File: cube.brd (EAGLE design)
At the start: 27.9 x 59.7 mm, 46 parts, among them CN1 4U#20329, IC3 ATSAMD21E, Q2 reset, U1 AP2112K-3.3

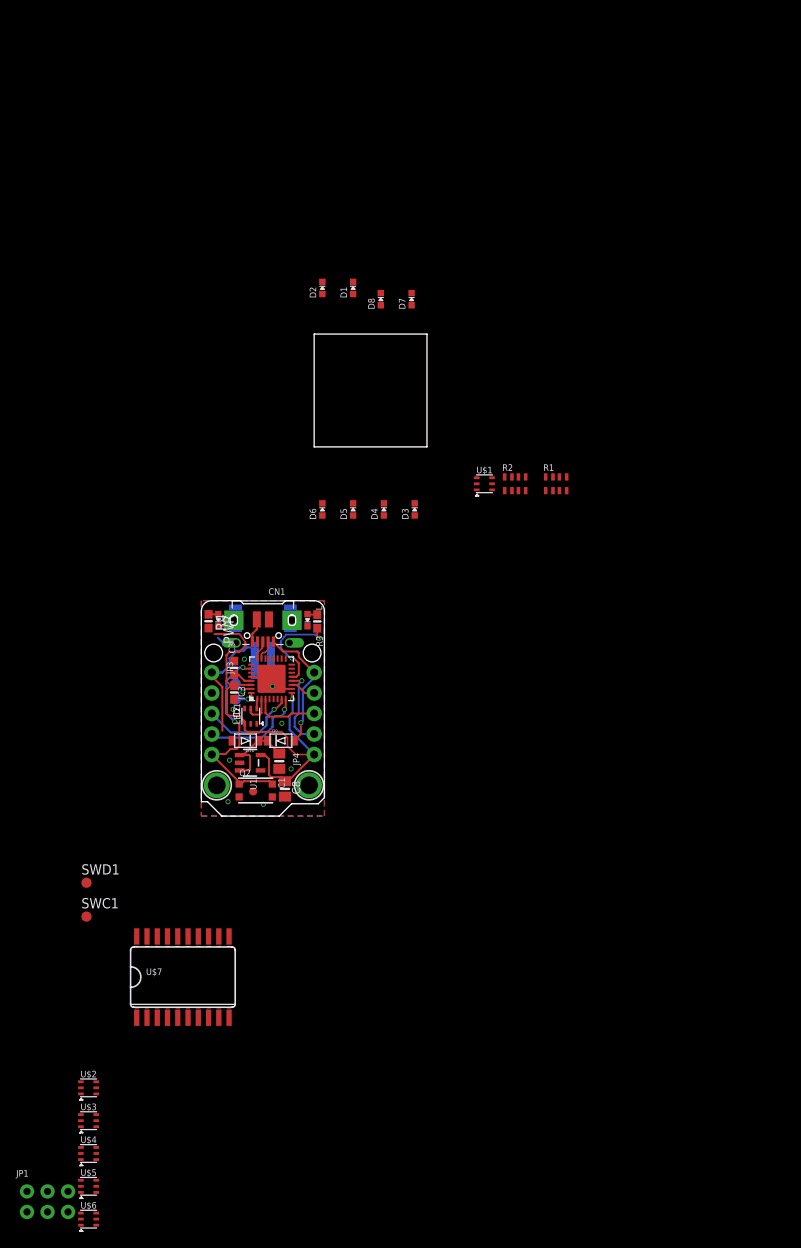
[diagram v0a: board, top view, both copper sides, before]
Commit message: made LED7 also a power led
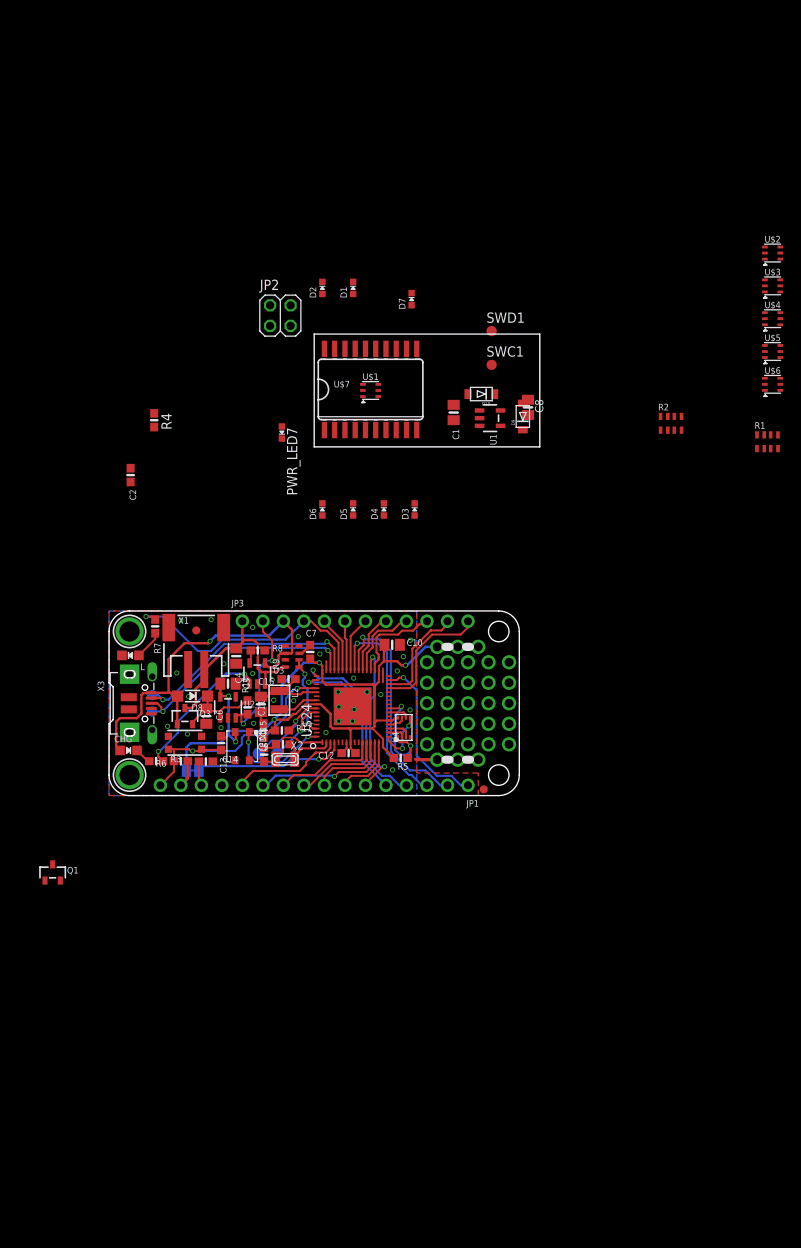
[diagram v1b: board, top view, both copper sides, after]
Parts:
- removed BAT: JST-2PH, microbuilder:JSTPH2
- removed CN1: 4U#20329, microbuilder:4UCONN_20329_V2
- removed IC3: ATSAMD21E, microbuilder:QFN32_5MM
- removed JP4: (no value), microbuilder:1X05_ROUND_76
- removed PWR: green, microbuilder:CHIPLED_0603_NOOUTLINE
- removed Q2: reset, microbuilder:BTN_KMR2_4.6X2.8
- removed SWC, SWD: TPB1,27, testpad:B1,27
- removed U$11, U$12: MOUNTINGHOLE2.0, microbuilder:MOUNTINGHOLE_2.0_PLATED
- removed U$22: (no value), microbuilder:PCBFEAT-REV-040
- removed U$23: (no value), silks:TRINKET_M0_TOP
- removed U$8: FIDUCIAL_1MM, microbuilder:FIDUCIAL_1MM
- added C10, C15: 10uF, microbuilder:0805-NO
- added C11, C12, C13, C14, C16, C7: 1uF, microbuilder:0603-NO
- added C4, C6: 10µF, microbuilder:0805-NO
- added C5, C9: 22pF, microbuilder:0603-NO
- added CHG: ORANGE, microbuilder:CHIPLED_0805_NOOUTLINE
- added D+, D-: TPB1,27, testpad:B1,27
- added JP2: (no value), pinhead:2X02
- added L2: 10uH, microbuilder:INDUCTOR_1007
- added PWR_LED7: green, microbuilder:CHIPLED_0603_NOOUTLINE
- added Q1, Q3: DMG341, microbuilder:SOT23-R
- added R10, R11, R5, R6: 10K, microbuilder:0603-NO
- added R7: 2.2K, microbuilder:0603-NO
- added R8: 10K\, microbuilder:0603-NO
- added R9: 100K, microbuilder:RESPACK_4X0603_NO
- added SJ1: (no value), microbuilder:SOLDERJUMPER_CLOSEDWIRE
- added SW1: KMR2, microbuilder:BTN_KMR2_4.6X2.8
- added TP1, TP2: (no value), microbuilder:TESTPOINT_ROUND_1.5MM
- added U$31, U$32: MOUNTINGHOLE2.5, microbuilder:MOUNTINGHOLE_2.5_PLATED
- added U$34, U$35: FIDUCIAL_1MM, microbuilder:FIDUCIAL_1MM
- added U$42: (no value), microbuilder:PCBFEAT-REV-040
- added U$43: (no value), silks:FEATHERM4_BOT
- added U$44: (no value), silks:FEATHERM4_TOP
- added U2: AP2112-3.3, microbuilder:SOT23-5
- added U3: MCP73831T-2ACI/OT, microbuilder:SOT23-5
- added U4: 2MB Flash, microbuilder:USON8
- added X1: JSTPH, microbuilder:JSTPH2
- added X2: 32.768, adafruit2:XTAL3215
- added X3: microUSB, microbuilder:4UCONN_20329_V2
- C3: value 1uF -> 10µF; device microbuilder:0603-NO -> microbuilder:0805-NO
- D8: value (none) -> MBR120; device microbuilder:CHIPLED_0603_NOOUTLINE -> microbuilder:SOD-123
- JP1: device microbuilder:2X03_ROUND_70MIL -> microbuilder:1X16_ROUND
- JP3: device microbuilder:1X05_ROUND_76 -> microbuilder:1X12_ROUND
- L: value red -> RED; device microbuilder:CHIPLED_0603_NOOUTLINE -> microbuilder:CHIPLED_0805_NOOUTLINE
- LED1: value AP102-2020 -> WS2812B3535; device microbuilder:APA102_2020 -> microbuilder:LED3535
- R3: value 1.5K -> 1K
- R4: value 10K -> 500
- U$24: value (none) -> ATSAMD51J; device silks:TRINKET_M0_BOTTOM -> microbuilder:PQFN64-1
- moved U$2 133.7 mm to (56.8, 24.0)
- moved U$4 133.7 mm to (56.8, 15.9)
- moved U$6 133.7 mm to (56.8, 7.75)
- moved U$3 133.7 mm to (56.8, 19.9)
- moved U$5 133.7 mm to (56.8, 11.8)
- moved SWD1 84.8 mm to (22.0, 14.4)
- moved SWC1 84.8 mm to (22.0, 10.2)
- moved U$7 76.4 mm to (6.99, 7.11)
- moved JP1 61.2 mm to (0.00, -41.9), turned to 180 degrees
- moved C8 56.0 mm to (26.5, 4.89)
- moved D8 54.4 mm to (-15.0, -30.9), turned to 180 degrees
- moved U1 52.0 mm to (21.8, 3.56)
- moved D10 51.9 mm to (20.7, 6.54)
- moved D9 50.1 mm to (25.8, 3.76), turned to 90 degrees
- moved C1 48.3 mm to (17.3, 4.25)
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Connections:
- net VOUT renamed VIN
- removed net D0_A4_PA08_SDA: IC3.11, JP4.4
- removed net D1_A0_PA02: IC3.3, JP4.3
- removed net D2_A1_PA09_SCL_MISO: IC3.12, JP4.2
- removed net D3_A3_PA07_RXD_SCK: IC3.8, JP3.4
- removed net D4_A2_PA06_TXD_MOSI: IC3.7, JP3.3
- removed net LED7: R2.4, U$7.20
- removed net LED_A7: D8.A, R2.5
- removed net N$6: PWR.A, R4.1
- removed net PA22/I2C/I6/X6/Y12/SERCOM1.0+2.0: U$7.9
- removed net SAO_GPIO1: JP1.1
- removed net SAO_GPIO2: JP1.2
- removed net VDDCORE: C3.1, IC3.29
- new net +3V3: C10.1, C11.1, C12.1, C3.1, C7.1, JP1.15, LED1.2, R11.1, R5.2, R6.1, SJ1.2, U$24.16, U$24.21, U$24.34, U$24.48, U$24.56, U$24.8, U2.5, U4.8
- new net A0: JP1.12, U$24.3
- new net A1: JP1.11, U$24.14
- new net A2: JP1.10, U$24.11
- new net A4: JP1.8, U$24.13
- new net A5: JP1.7, U$24.15
- new net AREF: C14.1, JP1.14, SJ1.1, U$24.4
- new net D10: JP3.7, U$24.41
- new net D11: JP3.6, U$24.42
- new net D12: JP3.5, U$24.43
- new net D13: JP3.4, R7.1, U$24.44
- new net D4: JP1.1, U$24.31
- new net D5: JP3.10, U$24.35
- new net D6: JP3.9, U$24.37
- new net D8_NEOPIX: LED1.1, U$24.64
- new net D9: JP3.8, U$24.38
- new net EN: JP3.2, R10.1, U2.3
- new net LED7_PWR: Q1.1, U$7.20
- new net MISO: JP1.4, U$24.49
- new net MOSI: JP1.5, U$24.50
- new net N$11: L2.P$2, U$24.55
- new net N$36: Q1.3, R4.1
- new net N$9: C9.1, U$24.2, X2.P$2
- new net QSPI_CS: R5.1, U$24.24, U4.1
- new net QSPI_DATA[0]: U$24.17, U4.5
- new net QSPI_DATA[1]: U$24.18, U4.2
- new net QSPI_DATA[2]: U$24.19, U4.3
- new net QSPI_DATA[3]: U$24.20, U4.7
- new net QSPI_SCK: U$24.23, U4.6
- new net RX_D0: JP1.3, U$24.40
- new net SCK: JP1.6, U$24.36
- new net SCL: JP3.11, U$24.30
- new net SDA: JP3.12, U$24.29
- new net SWCLK: R11.2, TP1.P$1, U$24.57
- new net SWDIO: TP2.P$1, U$24.58
- new net TX_D1: JP1.2, U$24.39
- new net VDDCORE1: C15.1, C16.1, L2.P$1, U$24.53
- new net VHI: C6.1, D8.C, Q3.2, R10.2, U2.1
- new net VHI1: PWR_LED7.A, Q1.2
- new net V_DIV: R9.1, R9.2, U$24.62
- net !RESET: now also C13.2, JP1.16, R6.2, SW1.A, SW1.A', U$24.52; no longer IC3.26, JP3.5, Q2.A, Q2.A'
- net 3.3V: no longer IC3.30, IC3.9, JP4.1, LED1.3
- net A3: now also JP1.9, U$24.12; no longer IC3.1, LED1.6
- net D+: now also D+.TP, U$24.46, X3.D+; no longer CN1.D+, IC3.24
- net D-: now also D-.TP, U$24.45, X3.D-; no longer CN1.D-, IC3.23
- net GND: now also C10.2, C11.2, C12.2, C13.1, C14.2, C15.2, C16.2, C4.2, C5.2, C6.2, C7.2, C9.2, JP1.13, JP2.1, PWR_LED7.C, R8.2, R9.3, R9.7, SW1.B, SW1.B', U$24.22, U$24.33, U$24.47, U$24.54, U$24.7, U$24.EXP, U2.2, U3.2, U4.4, X1.1, X3.BASE@1, X3.BASE@2, X3.GND, X3.SPRT@1, X3.SPRT@2, X3.SPRT@3, X3.SPRT@4; no longer BAT.1, CN1.BASE@1, CN1.BASE@2, CN1.GND, CN1.SPRT@1, CN1.SPRT@2, CN1.SPRT@3, CN1.SPRT@4, D8.C, IC3.10, IC3.28, IC3.33, JP1.6, JP3.2, PWR.C, Q2.B, Q2.B'
- net N$1: now also CHG.C; no longer L.A
- net N$2: now also L.A, R7.2; no longer IC3.13, R3.2
- net N$3: now also R3.2, U3.1; no longer IC3.31, SWC.TP
- net N$4: now also R8.1, U3.5; no longer IC3.32, SWD.TP
- net N$8: now also C5.1, U$24.1, X2.P$1; no longer IC3.2, LED1.5
- net SAO_SCL: now also JP2.3; no longer JP1.4
- net SAO_SDA: now also JP2.4; no longer JP1.3
- net SAO_VDD: now also JP2.2; no longer JP1.5
- net VBAT: now also C4.1, Q3.3, R9.8, U3.3, X1.2; no longer BAT.2
- net VBUS: now also CHG.A, D8.A, JP3.3, Q3.1, R9.6, U3.4, X3.VBUS; no longer CN1.VBUS, JP4.5
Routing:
- net +3V3: track 0.00 -> 104.9 mm, vias 0 -> 8
- net 3.3V: track 46.5 -> 0.00 mm, vias 1 -> 0
- net D13: track 0.00 -> 33.0 mm, vias 0 -> 1
- net VBUS: track 16.4 -> 47.5 mm
- net TX_D1: track 0.00 -> 29.8 mm, vias 0 -> 1
- net D-: track 2.57 -> 30.4 mm, vias 0 -> 2
- net D+: track 2.36 -> 30.0 mm, vias 0 -> 2
- net RX_D0: track 0.00 -> 26.7 mm, vias 0 -> 1
- net AREF: track 0.00 -> 24.5 mm, vias 0 -> 1
- net MISO: track 0.00 -> 22.8 mm, vias 0 -> 1
- net SCK: track 0.00 -> 20.2 mm, vias 0 -> 2
- net D4: track 0.00 -> 20.2 mm, vias 0 -> 1
- net MOSI: track 0.00 -> 20.2 mm, vias 0 -> 1
- net EN: track 0.00 -> 17.9 mm, vias 0 -> 2
- net A1: track 0.00 -> 17.7 mm, vias 0 -> 1
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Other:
- board size 27.9 x 59.7 mm -> 53.3 x 57.1 mm
- board text removed: "+"
- board text removed: "-"
- board text removed: "D0/A4/SDA"
- board text removed: "D1/A0/VOUT"
- board text removed: "D2/A1/SCL/MISO"
- board text removed: "D3/A3/TXD/SCK"
- board text removed: "D4/A2/RXD/MOSI"

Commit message: updtes with suggestion from cgrover
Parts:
- removed Q1: DMG341, microbuilder:SOT23-R
- added D12: (no value), microbuilder:SOD-323
- added Q2: (no value), microbuilder:SOT23-R
- added R12: 100K, microbuilder:0603-NO
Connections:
- new net N$6: D12.A, Q2.1, R12.1
- net LED7_PWR: now also D12.C; no longer Q1.1
- net N$36: now also Q2.2; no longer Q1.3
- net VDD: now also R12.2
- net VHI1: now also Q2.3; no longer Q1.2
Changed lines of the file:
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@@
 <element name="U$43" library="silks" package="FEATHERM4_BOT" value="" x="25.4" y="-43.18" smashed="yes" rot="MR0"/>
 <element name="U$44" library="silks" package="FEATHERM4_TOP" value="" x="-25.4" y="-43.18" smashed="yes"/>
-<element name="Q1" library="microbuilder" package="SOT23-R" value="DMG341" x="-32.385" y="-52.705" smashed="yes">
-<attribute name="NAME" x="-30.607" y="-52.832" size="0.8128" layer="25" ratio="18"/>
-<attribute name="VALUE" x="-30.607" y="-53.34" size="0.4064" layer="27" ratio="10"/>
+<element name="Q2" library="microbuilder" package="SOT23-R" value="" x="-32.385" y="-55.88" smashed="yes">
+<attribute name="NAME" x="-30.607" y="-56.007" size="0.8128" layer="25" ratio="18"/>
+<attribute name="VALUE" x="-30.607" y="-56.515" size="0.4064" layer="27" ratio="10"/>
+</element>
+<element name="R12" library="microbuilder" package="0603-NO" value="100K" x="-32.512" y="-58.547" smashed="yes">
+<attribute name="NAME" x="-30.734" y="-58.674" size="0.8128" layer="25" font="vector" ratio="18"/>
+<attribute name="VALUE" x="-30.734" y="-59.309" size="0.4064" layer="27" font="vector" ratio="10"/>
+</element>
+<element name="D12" library="microbuilder" package="SOD-323" value="" x="-32.004" y="-65.405" smashed="yes">
+<attribute name="NAME" x="-33.104" y="-64.405" size="0.8128" layer="25" ratio="18"/>
+<attribute name="VALUE" x="-33.104" y="-67.197" size="0.4064" layer="27" ratio="10"/>
 </element>
 </elements>
@@
 <contactref element="U$6" pad="3"/>
 <contactref element="R4" pad="2"/>
-<wire x1="55.819" y1="20.689" x2="55.819" y2="24.753" width="0" layer="19" extent="1-1"/>
-<wire x1="55.819" y1="16.625" x2="55.819" y2="20.689" width="0" layer="19" extent="1-1"/>
-<wire x1="55.819" y1="12.561" x2="55.819" y2="16.625" width="0" layer="19" extent="1-1"/>
-<wire x1="55.819" y1="8.497" x2="55.819" y2="12.561" width="0" layer="19" extent="1-1"/>
-<wire x1="26.4795" y1="5.8395" x2="55.819" y2="8.497" width="0" layer="19" extent="1-1"/>
-<wire x1="23.0806" y1="4.506" x2="26.4795" y2="5.8395" width="0" layer="19" extent="1-1"/>
-<wire x1="6.035" y1="7.735" x2="23.0806" y2="4.506" width="0" layer="19" extent="1-1"/>
+<contactref element="R12" pad="2"/>
+<wire x1="-19.812" y1="2.452" x2="-31.662" y2="-58.547" width="0" layer="19" extent="1-1"/>
+<wire x1="6.035" y1="7.735" x2="-19.812" y2="2.452" width="0" layer="19" extent="1-1"/>
 <wire x1="5.08" y1="12.1412" x2="6.035" y2="7.735" width="0" layer="19" extent="1-1"/>
-<wire x1="-19.812" y1="2.452" x2="6.035" y2="7.735" width="0" layer="19" extent="1-1"/>
+<wire x1="23.0806" y1="4.506" x2="6.035" y2="7.735" width="0" layer="19" extent="1-1"/>
+<wire x1="26.4795" y1="5.8395" x2="23.0806" y2="4.506" width="0" layer="19" extent="1-1"/>
+<wire x1="55.819" y1="8.497" x2="26.4795" y2="5.8395" width="0" layer="19" extent="1-1"/>
+<wire x1="55.819" y1="12.561" x2="55.819" y2="8.497" width="0" layer="19" extent="1-1"/>
+<wire x1="55.819" y1="16.625" x2="55.819" y2="12.561" width="0" layer="19" extent="1-1"/>
+<wire x1="55.819" y1="20.689" x2="55.819" y2="16.625" width="0" layer="19" extent="1-1"/>
+<wire x1="55.819" y1="24.753" x2="55.819" y2="20.689" width="0" layer="19" extent="1-1"/>
 </signal>
 <signal name="CKO1">
@@
 </signal>
 <signal name="VHI1">
-<contactref element="Q1" pad="2"/>
 <contactref element="PWR_LED7" pad="A"/>
-<wire x1="-4.0005" y1="2.528" x2="-31.435" y2="-53.705" width="0" layer="19" extent="1-1"/>
+<contactref element="Q2" pad="3"/>
+<wire x1="-4.0005" y1="2.528" x2="-32.385" y2="-54.88" width="0" layer="19" extent="1-1"/>
 </signal>
 <signal name="LED7_PWR">
 <contactref element="U$7" pad="20"/>
-<contactref element="Q1" pad="1"/>
-<wire x1="1.27" y1="12.1412" x2="-33.335" y2="-53.705" width="0" layer="19" extent="1-1"/>
+<contactref element="D12" pad="C"/>
+<wire x1="1.27" y1="12.1412" x2="-33.274" y2="-65.405" width="0" layer="19" extent="1-1"/>
 </signal>
 <signal name="N$36" class="1">
-<contactref element="Q1" pad="3"/>
 <contactref element="R4" pad="1"/>
-<wire x1="-19.812" y1="4.152" x2="-32.385" y2="-51.705" width="0" layer="19" extent="1-1"/>
+<contactref element="Q2" pad="2"/>
+<wire x1="-19.812" y1="4.152" x2="-31.435" y2="-56.88" width="0" layer="19" extent="1-1"/>
+</signal>
+<signal name="N$6">
+<contactref element="Q2" pad="1"/>
+<contactref element="R12" pad="1"/>
+<contactref element="D12" pad="A"/>
+<wire x1="-33.362" y1="-58.547" x2="-30.734" y2="-65.405" width="0" layer="19" extent="1-1"/>
+<wire x1="-33.335" y1="-56.88" x2="-33.362" y2="-58.547" width="0" layer="19" extent="1-1"/>
 </signal>
 </signals>
